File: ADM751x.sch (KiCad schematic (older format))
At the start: 6 parts, among them U3 ADM7514

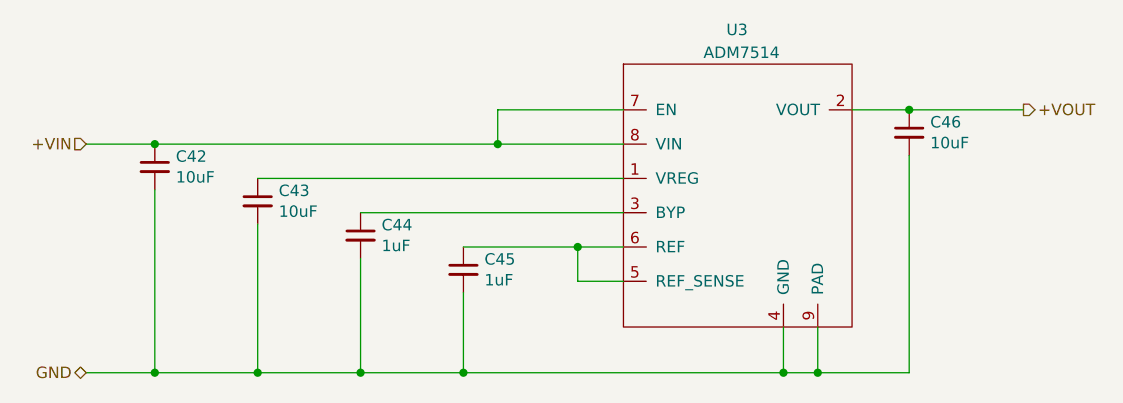
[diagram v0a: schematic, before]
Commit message: finsihed traces for one EC sensor
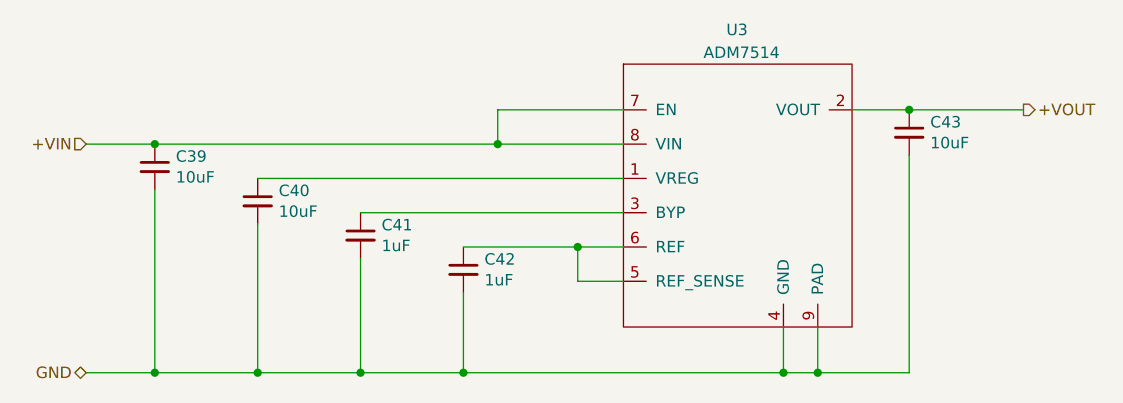
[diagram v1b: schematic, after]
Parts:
- renumbered C42 to C39, C43 to C40, C44 to C41, C45 to C42, C46 to C43
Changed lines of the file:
@@
 $EndDescr
 $Comp
-L Device:C_Small C45
+L Device:C_Small C42
 U 1 1 600F29C3
 P 4850 5150
-F 0 "C45" H 4942 5196 50  0000 L CNN
+F 0 "C42" H 4942 5196 50  0000 L CNN
 F 1 "1uF" H 4942 5105 50  0000 L CNN
 F 2 "Capacitor_SMD:C_0402_1005Metric" H 4850 5150 50  0001 C CNN
@@
 $EndComp
 $Comp
-L Device:C_Small C44
+L Device:C_Small C41
 U 1 1 600F314F
 P 4400 5000
-F 0 "C44" H 4492 5046 50  0000 L CNN
+F 0 "C41" H 4492 5046 50  0000 L CNN
 F 1 "1uF" H 4492 4955 50  0000 L CNN
 F 2 "Capacitor_SMD:C_0402_1005Metric" H 4400 5000 50  0001 C CNN
@@
 $EndComp
 $Comp
-L Device:C_Small C43
+L Device:C_Small C40
 U 1 1 600F3438
 P 3950 4850
-F 0 "C43" H 4042 4896 50  0000 L CNN
+F 0 "C40" H 4042 4896 50  0000 L CNN
 F 1 "10uF" H 4042 4805 50  0000 L CNN
 F 2 "Capacitor_SMD:C_0402_1005Metric" H 3950 4850 50  0001 C CNN
@@
 $EndComp
 $Comp
-L Device:C_Small C46
+L Device:C_Small C43
 U 1 1 600F3B6B
 P 6800 4550
-F 0 "C46" H 6892 4596 50  0000 L CNN
+F 0 "C43" H 6892 4596 50  0000 L CNN
 F 1 "10uF" H 6892 4505 50  0000 L CNN
 F 2 "Capacitor_SMD:C_0402_1005Metric" H 6800 4550 50  0001 C CNN
@@
 $EndComp
 $Comp
-L Device:C_Small C42
+L Device:C_Small C39
 U 1 1 600F3DC9
 P 3500 4700
-F 0 "C42" H 3592 4746 50  0000 L CNN
+F 0 "C39" H 3592 4746 50  0000 L CNN
 F 1 "10uF" H 3592 4655 50  0000 L CNN
 F 2 "Capacitor_SMD:C_0402_1005Metric" H 3500 4700 50  0001 C CNN

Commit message: first draft done, needs reviewing
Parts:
- U3: footprint Package_CSP:Analog_LFCSP-8-1EP_3x3mm_P0.5mm_EP1.53x1.85mm -> SIB_Generic:LFCSP_8Lead_CP_8_21
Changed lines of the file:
@@
 U 1 1 600FF2A9
 P 6050 4750
+AR Path="/600FF2A9" Ref="U3"  Part="1"
+AR Path="/600E8F3B/600FF2A9" Ref="U3"  Part="1"
 F 0 "U3" H 6000 5400 50  0000 L CNN
 F 1 "ADM7514" H 5900 5300 50  0000 L CNN
-F 2 "Package_CSP:Analog_LFCSP-8-1EP_3x3mm_P0.5mm_EP1.53x1.85mm" H 3800 6500 50  0001 C CNN
+F 2 "SIB_Generic:LFCSP_8Lead_CP_8_21" H 3800 6500 50  0001 C CNN
 F 3 "" H 3800 6500 50  0001 C CNN
 	1    6050 4750
